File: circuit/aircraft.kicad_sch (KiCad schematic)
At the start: 22 parts, among them SW1 SW_Push_Dual, SW10 SW_Push_Dual, SW2 SW_Push_Dual, SW3 SW_Push_Dual, SW4 SW_Push_Dual, SW5 SW_Push_Dual, SW6 SW_Push_Dual, SW7 SW_Push_Dual, SW8 SW_Push_Dual, SW9 SW_Push_Dual, U1 MCP23017_SP, U2 ESP32, U3 nRF24L01, U4 LCD_Display_20x4, U5 LCD_I2C_Serial, U6 AMS1117-3.3, U7 Joystick_Hall_XY, U8 Joystick_Hall_XY

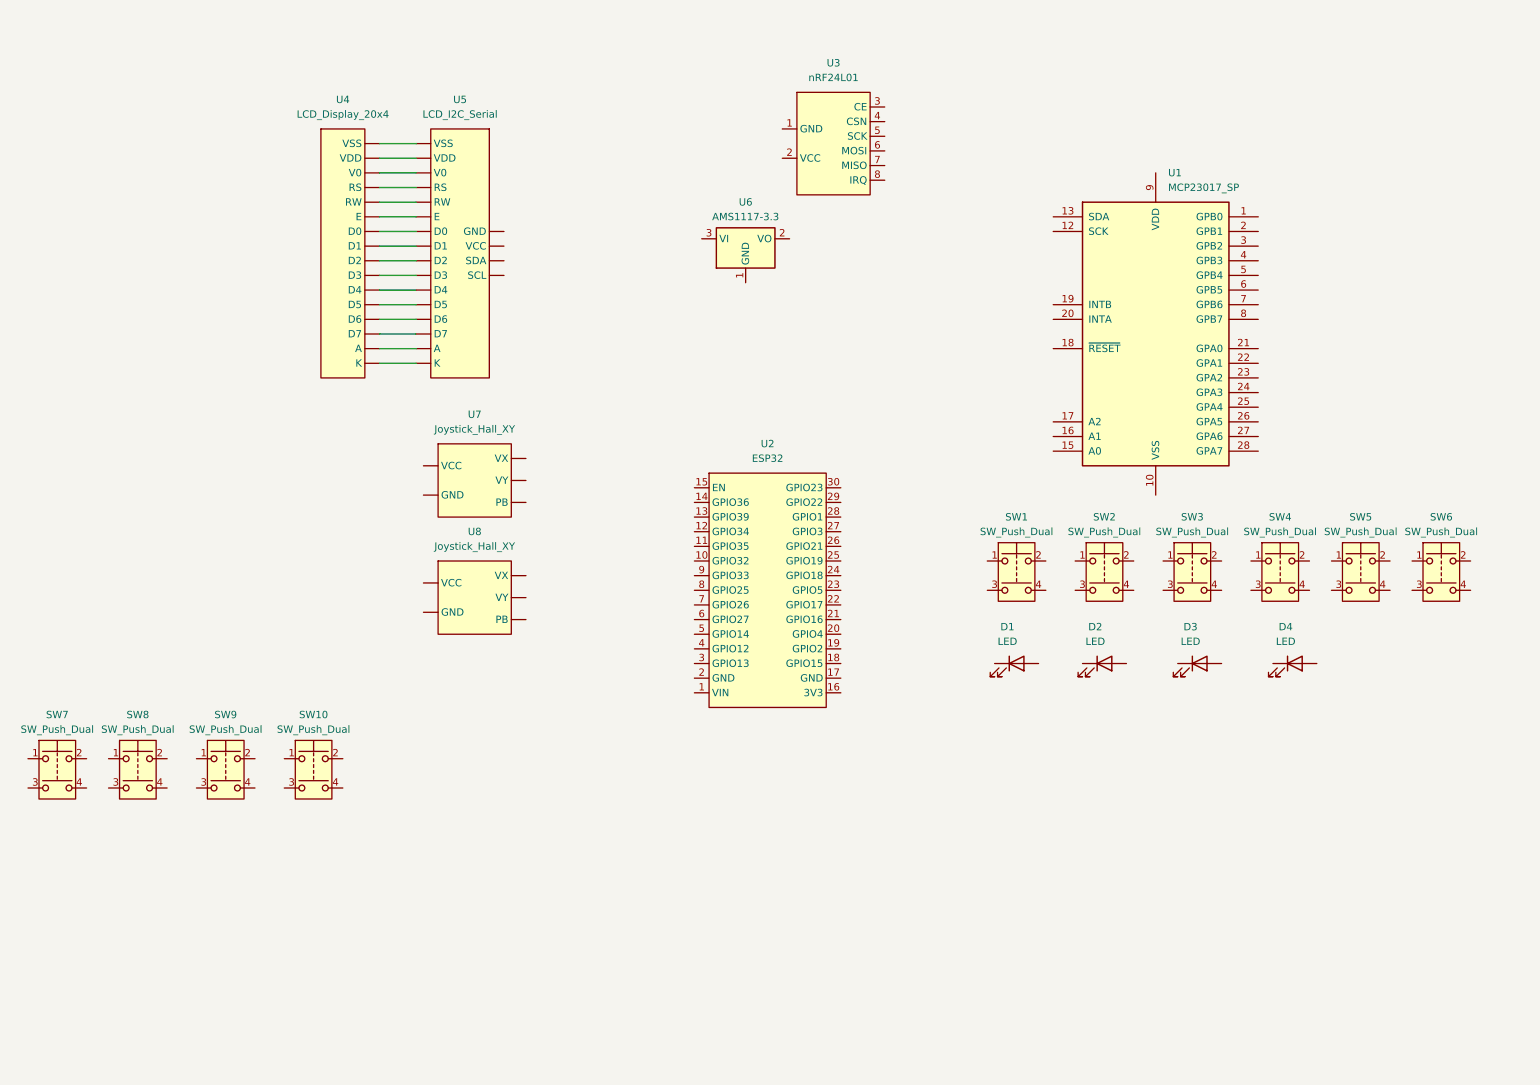
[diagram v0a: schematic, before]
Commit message: control circuit finished, control menu code finished
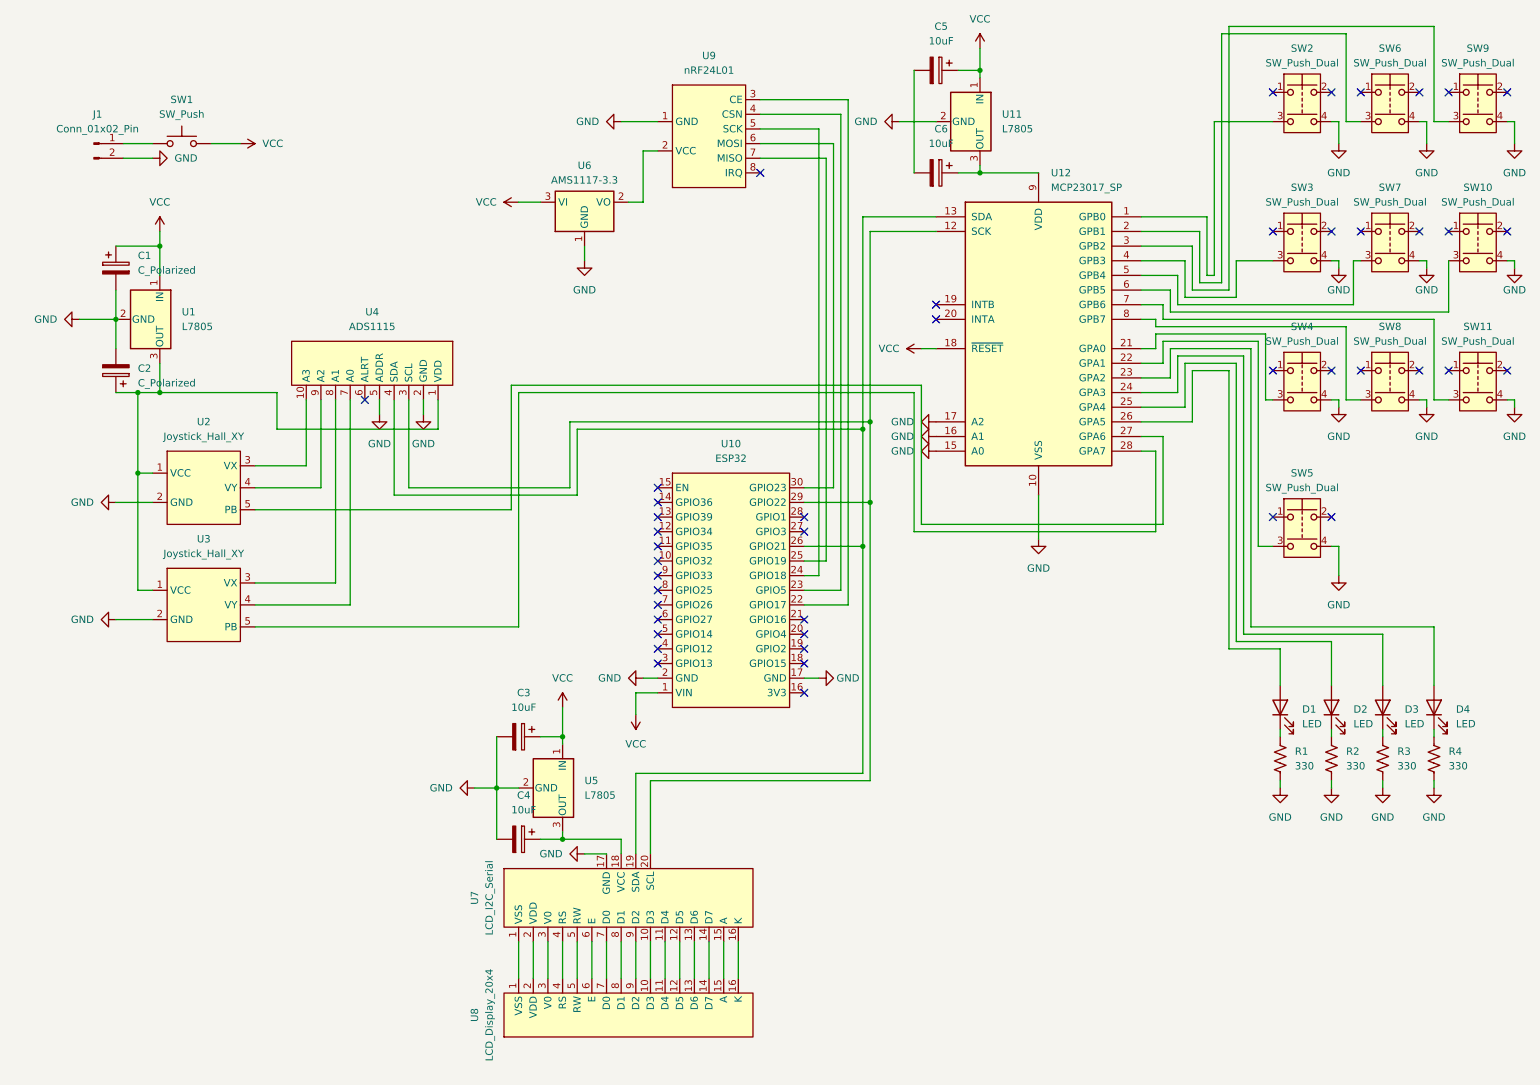
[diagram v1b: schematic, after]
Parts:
- added C1, C2: C_Polarized, symbol Device:C_Polarized
- added C3, C4, C5, C6: 10uF, symbol Device:C_Polarized
- added J1: Conn_01x02_Pin, symbol Connector:Conn_01x02_Pin
- added R1, R2, R3, R4: 330, symbol Device:R_US
- added SW1: SW_Push, symbol Switch:SW_Push
- added U1, U11, U5: L7805, symbol Regulator_Linear:L7805
- added U4: ADS1115, symbol Aircraft_Components:ADS1115
- renumbered D4 to D1, D3 to D2, D2 to D3, D1 to D4, SW6 to SW10, SW9 to SW11, SW1 to SW2, SW4 to SW3, SW7 to SW4, SW10 to SW5, SW2 to SW6, SW5 to SW7, SW3 to SW9, U2 to U10, U1 to U12, U7 to U2, U8 to U3, U5 to U7, U4 to U8, U3 to U9
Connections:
- net at SW7.3: now also U12.5 (GPB4)
- net GND: now reaches SW7.4
- net GND: now also SW10.4, SW11.4, SW2.4, SW3.4, SW4.4, SW5.4, SW6.4, SW8.4, SW9.4, U10.17 (GND), U10.2 (GND), U12.10 (VSS), U12.15 (A0), U12.16 (A1), U12.17 (A2), U2.2 (GND), U3.2 (GND), U6.1 (GND), U7.17 (GND), U9.1 (GND), C1.2, C2.2, C3.2, C4.2, J1.2 (Pin_2), R1.2, R2.2, R3.2, R4.2, U1.2 (GND), U11.2 (GND), U4.2 (GND), U4.5 (ADDR), U5.2 (GND)
- net at D3.1 (K): now also R3.1
- net at D3.2 (A): now also U12.24 (GPA3)
- net at U9.2 (VCC): now also U6.2 (VO)
- net at U9.3 (CE): now also U10.22 (GPIO17)
- net at U9.4 (CSN): now also U10.23 (GPIO5)
- net at U9.5 (SCK): now also U10.24 (GPIO18)
- net at U9.6 (MOSI): now also U10.30 (GPIO23)
- net at U9.7 (MISO): now also U10.25 (GPIO19)
- net at SW11.3: now also U12.7 (GPB6)
- net at D1.1 (K): now also R1.1
- net at D1.2 (A): now also U12.26 (GPA5)
- net at SW3.3: now also U12.4 (GPB3)
- net at U12.1 (GPB0): now also SW2.3
- net at U12.12 (SCK): now also U10.29 (GPIO22), U7.20 (SCL), U4.3 (SCL)
- net at U12.13 (SDA): now also U10.26 (GPIO21), U7.19 (SDA), U4.4 (SDA)
- net VCC: now reaches U12.18 (~{RESET})
- net VCC: now also U10.1 (VIN), U6.3 (VI), C1.1, C3.1, C5.1, SW1.2, U1.1 (IN), U11.1 (IN), U5.1 (IN)
- net at U12.2 (GPB1): now also SW6.3
- net at U12.21 (GPA0): now also SW4.3
- net at U12.22 (GPA1): now also SW5.3
- net at U12.23 (GPA2): now also D4.2 (A)
- net at U12.25 (GPA4): now also D2.2 (A)
- net at U12.27 (GPA6): now also U2.5 (PB)
- net at U12.28 (GPA7): now also U3.5 (PB)
- net at U12.3 (GPB2): now also SW9.3
- net at U12.6 (GPB5): now also SW10.3
- net at U12.8 (GPB7): now also SW8.3
- net at U12.9 (VDD): now also C6.1, U11.3 (OUT)
- net at D2.1 (K): now also R2.1
- net at D4.1 (K): now also R4.1
- new net: C4.1, U5.3 (OUT), U7.18 (VCC)
- new net: C2.1, U1.3 (OUT), U2.1 (VCC), U3.1 (VCC), U4.1 (VDD)
- new net: U2.3 (VX), U4.10 (A3)
- new net: U3.4 (VY), U4.7 (A0)
- new net: U3.3 (VX), U4.8 (A1)
- new net: U2.4 (VY), U4.9 (A2)
- new net: J1.1 (Pin_1), SW1.1
- new net: U7.1 (VSS), U8.1 (VSS)
- new net: U7.10 (D3), U8.10 (D3)
- new net: U7.11 (D4), U8.11 (D4)
- new net: U7.12 (D5), U8.12 (D5)
- new net: U7.13 (D6), U8.13 (D6)
- new net: U7.14 (D7), U8.14 (D7)
- new net: U7.15 (A), U8.15 (A)
- new net: U7.16 (K), U8.16 (K)
- new net: U7.2 (VDD), U8.2 (VDD)
- new net: U7.3 (V0), U8.3 (V0)
- new net: U7.4 (RS), U8.4 (RS)
- new net: U7.5 (RW), U8.5 (RW)
- new net: U7.6 (E), U8.6 (E)
- new net: U7.7 (D0), U8.7 (D0)
- new net: U7.8 (D1), U8.8 (D1)
- new net: U7.9 (D2), U8.9 (D2)
- new net: C5.2, C6.2
- no-connect marks 0 -> 44
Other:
- company: (none) -> Breno Soares Alves
- title: (none) -> Remote Control
- moved on the sheet: D1, D2, D3, D4, SW10, SW11, SW2, SW3, SW4, SW5, SW6, SW7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
